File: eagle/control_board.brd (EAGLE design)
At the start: 160 x 100 mm, 24 parts, among them Q1 TIP122V

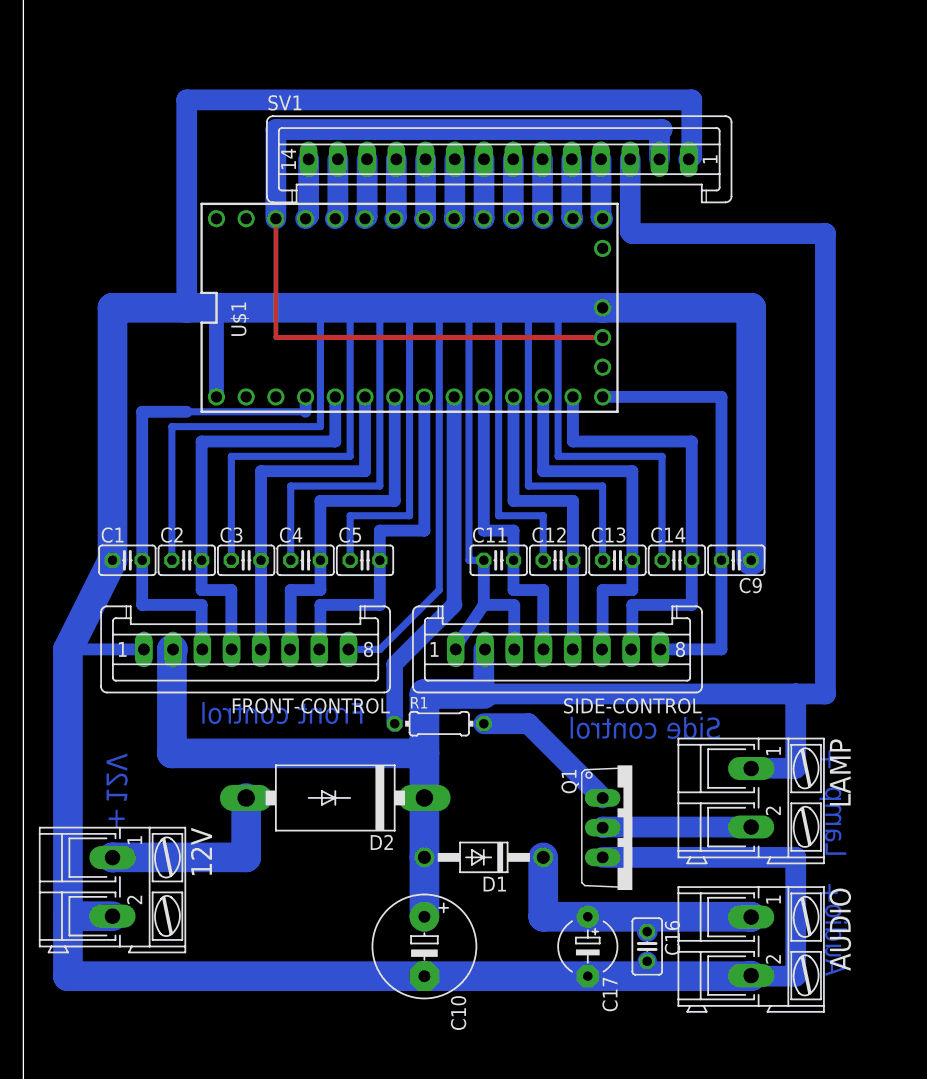
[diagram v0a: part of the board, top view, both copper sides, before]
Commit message: Add USB copy + several bug fix
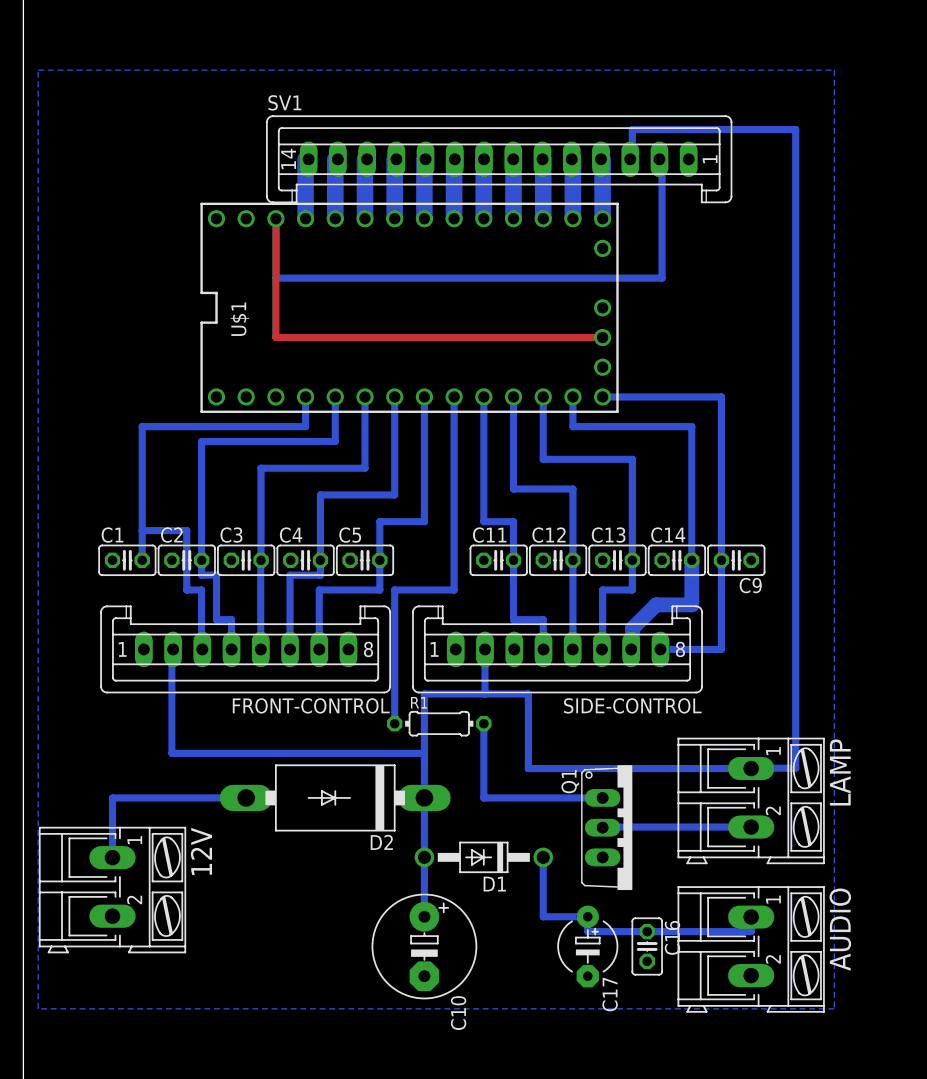
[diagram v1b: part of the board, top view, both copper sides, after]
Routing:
- net GND: track 586.2 -> 0.00 mm
- net +5V: track 81.4 -> 86.6 mm
- net N$1: track 12.8 -> 16.5 mm
- net LAMP: track 30.0 -> 33.0 mm
- net +12V: track 160.2 -> 162.9 mm
- net BTN_PHOTO: track 40.7 -> 43.2 mm
- net N$2: track 24.2 -> 25.4 mm
- net BTN_GAME: track 36.9 -> 35.7 mm
- added copper zone on layer 16, net GND
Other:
- board text removed: "+"
- board text removed: "12V"
- board text removed: "Audio"
- board text removed: "Front control"
- board text removed: "Lamp"
- board text removed: "Side control"

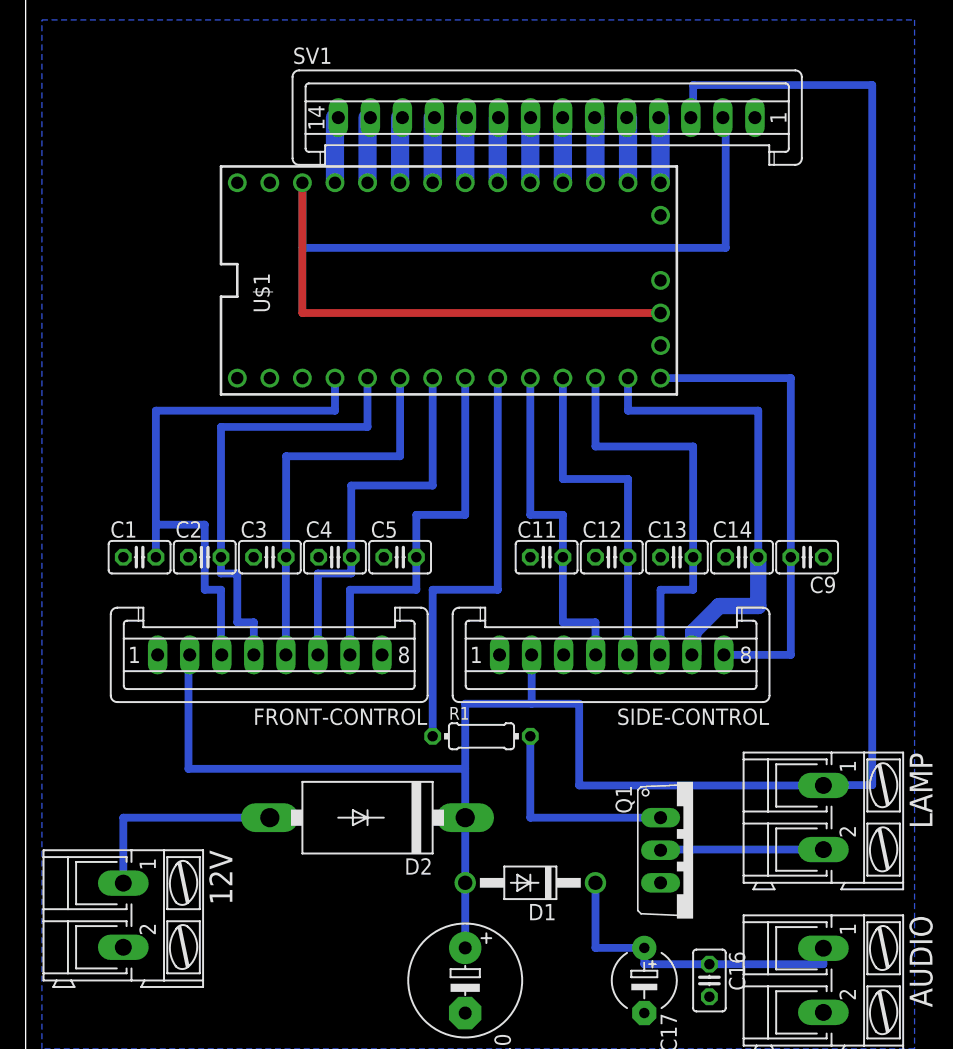
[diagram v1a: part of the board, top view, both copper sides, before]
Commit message: Working form & light control
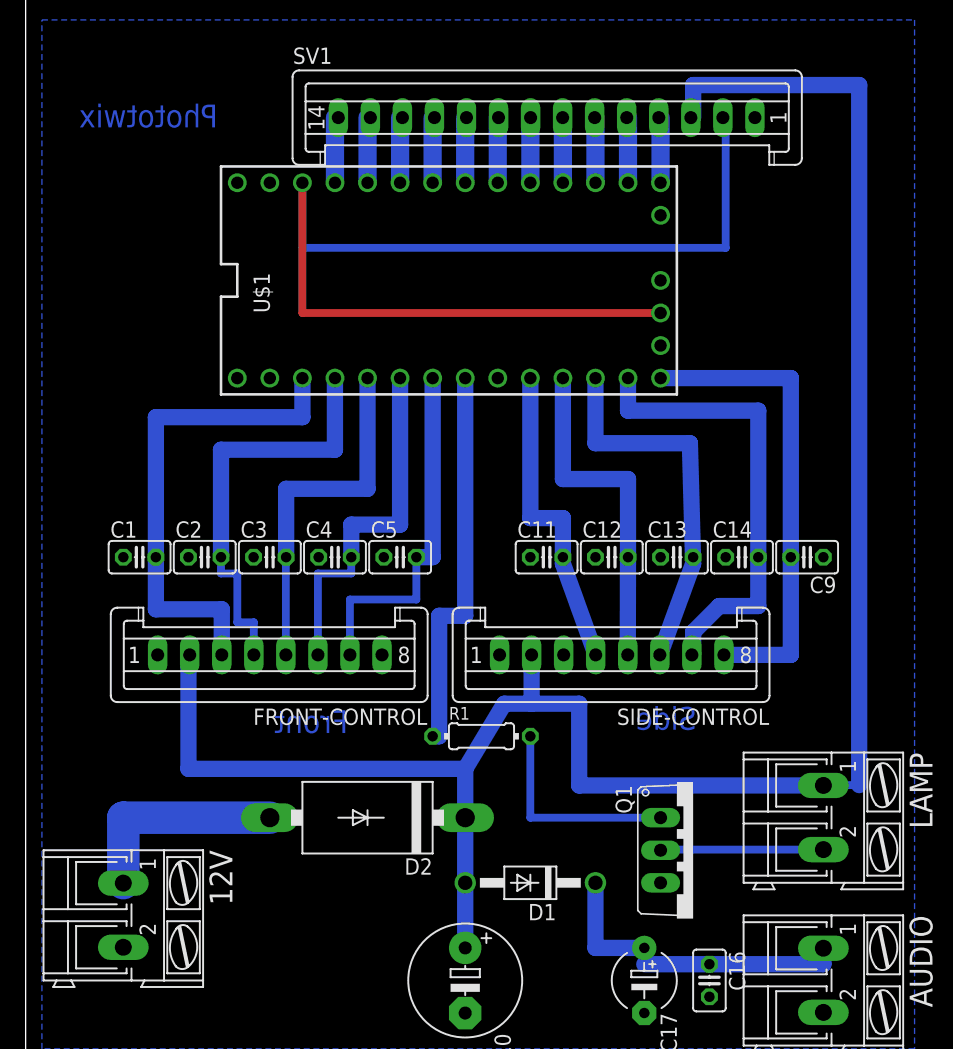
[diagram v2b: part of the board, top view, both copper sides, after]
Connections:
- net BTN_GALLERY: now also U$1.5; no longer U$1.6
- net BTN_NEXT: now also U$1.2; no longer U$1.3
- net BTN_PHOTO: now also U$1.1; no longer U$1.2
- net BTN_PREV: now also U$1.3; no longer U$1.4
- net BTN_TEMPLATE: now also U$1.4; no longer U$1.5
- net LAMP: now also U$1.6; no longer U$1.7
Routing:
- net BTN_PHOTO: track 43.2 -> 38.2 mm
- net +12V: track 162.9 -> 158.7 mm
- net LAMP: track 33.0 -> 30.5 mm
- net BTN_TEMPLATE: track 30.5 -> 28.0 mm
- net BTN_PREV: track 30.5 -> 28.0 mm
- net BTN_NEXT: track 35.6 -> 33.0 mm
- net BTN_GALLERY: track 30.6 -> 28.0 mm
- net BTN_USB: track 31.8 -> 30.0 mm
- net BTN_PRINT: track 26.7 -> 25.1 mm
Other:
- board text added: "Front"
- board text added: "Phototwix"
- board text added: "Side"

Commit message: Autocad plan
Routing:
- net GND: track 0.00 -> 516.1 mm
- net BTN_GALLERY: track 28.0 -> 26.2 mm
- removed copper zone on layer 16, net GND
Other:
- board text added: "12V+"
- board text added: "Audio"
- board text added: "Light+"
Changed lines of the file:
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@@
 <layer number="19" name="Unrouted" color="6" fill="1" visible="yes" active="yes"/>
 <layer number="20" name="Dimension" color="15" fill="1" visible="no" active="yes"/>
-<layer number="21" name="tPlace" color="7" fill="1" visible="yes" active="yes"/>
+<layer number="21" name="tPlace" color="7" fill="1" visible="no" active="yes"/>
 <layer number="22" name="bPlace" color="7" fill="1" visible="no" active="yes"/>
-<layer number="23" name="tOrigins" color="15" fill="1" visible="yes" active="yes"/>
+<layer number="23" name="tOrigins" color="15" fill="1" visible="no" active="yes"/>
 <layer number="24" name="bOrigins" color="15" fill="1" visible="no" active="yes"/>
 <layer number="25" name="tNames" color="7" fill="1" visible="no" active="yes"/>
@@
 <text x="25.146" y="35.814" size="1.778" layer="16" rot="MR0">Front</text>
 <text x="52.324" y="36.068" size="1.778" layer="16" rot="MR0">Side</text>
+<text x="19.304" y="23.368" size="1.778" layer="16" rot="MR0">12V+</text>
+<text x="68.58" y="18.796" size="1.778" layer="16" rot="MR270">Audio</text>
+<text x="68.58" y="29.718" size="1.778" layer="16" rot="MR270">Light+</text>
 </plain>
 <attributes>
@@
 <contactref element="SV1" pad="1"/>
 <contactref element="SIDE-CONTROL" pad="3"/>
-<polygon width="0.6096" layer="16">
-<vertex x="1.27" y="91.44"/>
-<vertex x="69.342" y="91.44"/>
-<vertex x="69.342" y="11.176"/>
-<vertex x="1.27" y="11.176"/>
-</polygon>
+<wire x1="56.89" y1="83.82" x2="57.15" y2="83.82" width="1.27" layer="16"/>
+<wire x1="57.15" y1="83.82" x2="57.15" y2="71.12" width="1.27" layer="16"/>
+<wire x1="57.15" y1="71.12" x2="49.53" y2="71.12" width="1.27" layer="16"/>
+<wire x1="49.53" y1="71.12" x2="45.72" y2="71.12" width="1.27" layer="16"/>
+<wire x1="45.72" y1="71.12" x2="43.18" y2="71.12" width="1.27" layer="16"/>
+<wire x1="43.18" y1="71.12" x2="40.64" y2="71.12" width="1.27" layer="16"/>
+<wire x1="40.64" y1="71.12" x2="35.56" y2="71.12" width="1.27" layer="16"/>
+<wire x1="35.56" y1="71.12" x2="33.02" y2="71.12" width="1.27" layer="16"/>
+<wire x1="33.02" y1="71.12" x2="30.48" y2="71.12" width="1.27" layer="16"/>
+<wire x1="30.48" y1="71.12" x2="27.94" y2="71.12" width="1.27" layer="16"/>
+<wire x1="27.94" y1="71.12" x2="25.4" y2="71.12" width="1.27" layer="16"/>
+<wire x1="25.4" y1="71.12" x2="22.86" y2="71.12" width="1.27" layer="16"/>
+<wire x1="22.86" y1="71.12" x2="16.51" y2="71.12" width="1.27" layer="16"/>
+<wire x1="16.51" y1="71.12" x2="16.51" y2="63.5" width="1.27" layer="16"/>
+<wire x1="7.62" y1="49.53" x2="7.366" y2="49.53" width="1.27" layer="16"/>
+<wire x1="7.366" y1="49.53" x2="7.366" y2="71.12" width="1.27" layer="16"/>
+<wire x1="7.366" y1="71.12" x2="16.51" y2="71.12" width="1.27" layer="16"/>
+<wire x1="62.23" y1="49.53" x2="62.23" y2="71.12" width="1.27" layer="16"/>
+<wire x1="62.23" y1="71.12" x2="57.15" y2="71.12" width="1.27" layer="16"/>
+<wire x1="34.29" y1="13.97" x2="48.26" y2="13.97" width="1.27" layer="16"/>
+<wire x1="48.26" y1="13.97" x2="53.34" y2="13.97" width="1.27" layer="16"/>
+<wire x1="53.34" y1="14.0208" x2="53.34" y2="15.24" width="1.27" layer="16"/>
+<wire x1="62.23" y1="14.0208" x2="53.34" y2="14.0208" width="1.27" layer="16"/>
+<wire x1="53.34" y1="14.0208" x2="53.34" y2="13.97" width="1.27" layer="16"/>
+<wire x1="39.37" y1="49.53" x2="36.97" y2="49.53" width="1.27" layer="16"/>
+<wire x1="36.97" y1="49.53" x2="36.97" y2="45.974" width="1.27" layer="16"/>
+<wire x1="36.97" y1="45.974" x2="36.97" y2="41.91" width="1.27" layer="16"/>
+<wire x1="49.53" y1="24.13" x2="65.278" y2="24.13" width="1.27" layer="16"/>
+<wire x1="65.278" y1="24.13" x2="65.278" y2="14.224" width="1.27" layer="16"/>
+<wire x1="65.278" y1="14.224" x2="62.23" y2="14.224" width="1.27" layer="16"/>
+<wire x1="62.23" y1="14.224" x2="62.23" y2="14.0208" width="1.27" layer="16"/>
+<wire x1="10.3" y1="41.91" x2="7.62" y2="41.91" width="1.27" layer="16"/>
+<wire x1="7.62" y1="41.91" x2="7.62" y2="49.53" width="1.27" layer="16"/>
+<wire x1="12.7" y1="49.53" x2="12.7" y2="59.436" width="0.4064" layer="16"/>
+<wire x1="12.7" y1="59.436" x2="22.86" y2="59.436" width="0.4064" layer="16"/>
+<wire x1="22.86" y1="59.436" x2="22.86" y2="71.12" width="0.4064" layer="16"/>
+<wire x1="17.78" y1="49.53" x2="17.78" y2="56.642" width="0.4064" layer="16"/>
+<wire x1="17.78" y1="56.642" x2="25.4" y2="56.642" width="0.4064" layer="16"/>
+<wire x1="25.4" y1="56.642" x2="25.4" y2="71.12" width="0.4064" layer="16"/>
+<wire x1="22.86" y1="49.53" x2="22.86" y2="53.594" width="0.4064" layer="16"/>
+<wire x1="22.86" y1="53.594" x2="27.94" y2="53.594" width="0.4064" layer="16"/>
+<wire x1="27.94" y1="53.594" x2="27.94" y2="71.12" width="0.4064" layer="16"/>
+<wire x1="27.94" y1="49.53" x2="27.94" y2="50.8" width="0.4064" layer="16"/>
+<wire x1="27.94" y1="50.8" x2="30.48" y2="50.8" width="0.4064" layer="16"/>
+<wire x1="30.48" y1="50.8" x2="30.48" y2="71.12" width="0.4064" layer="16"/>
+<wire x1="27.8" y1="41.91" x2="30.48" y2="41.91" width="0.4064" layer="16"/>
+<wire x1="30.48" y1="41.91" x2="30.48" y2="47.244" width="0.4064" layer="16"/>
+<wire x1="30.48" y1="47.244" x2="33.02" y2="47.244" width="0.4064" layer="16"/>
+<wire x1="33.02" y1="47.244" x2="33.02" y2="71.12" width="0.4064" layer="16"/>
+<wire x1="36.97" y1="49.53" x2="35.56" y2="50.94" width="0.4064" layer="16"/>
+<wire x1="35.56" y1="50.94" x2="35.56" y2="71.12" width="0.4064" layer="16"/>
+<wire x1="41.97" y1="41.91" x2="41.97" y2="43.882" width="0.4064" layer="16"/>
+<wire x1="41.97" y1="43.882" x2="40.132" y2="45.72" width="0.4064" layer="16"/>
+<wire x1="40.132" y1="45.72" x2="37.224" y2="45.72" width="0.4064" layer="16"/>
+<wire x1="37.224" y1="45.72" x2="36.97" y2="45.974" width="0.4064" layer="16"/>
+<wire x1="44.45" y1="49.53" x2="44.45" y2="54.102" width="0.4064" layer="16"/>
+<wire x1="44.45" y1="54.102" x2="40.64" y2="54.102" width="0.4064" layer="16"/>
+<wire x1="40.64" y1="54.102" x2="40.64" y2="71.12" width="0.4064" layer="16"/>
+<wire x1="49.53" y1="49.53" x2="49.53" y2="56.896" width="0.4064" layer="16"/>
+<wire x1="49.53" y1="56.896" x2="43.18" y2="56.896" width="0.4064" layer="16"/>
+<wire x1="43.18" y1="56.896" x2="43.18" y2="71.12" width="0.4064" layer="16"/>
+<wire x1="54.61" y1="49.53" x2="54.61" y2="59.69" width="0.4064" layer="16"/>
+<wire x1="54.61" y1="59.69" x2="45.72" y2="59.69" width="0.4064" layer="16"/>
+<wire x1="45.72" y1="59.69" x2="45.72" y2="71.12" width="0.4064" layer="16"/>
+<wire x1="7.62" y1="19.1008" x2="4.064" y2="19.05" width="1.27" layer="16"/>
+<wire x1="4.064" y1="19.05" x2="4.064" y2="41.91" width="1.27" layer="16"/>
+<wire x1="4.064" y1="41.91" x2="7.62" y2="41.91" width="1.27" layer="16"/>
+<wire x1="34.29" y1="13.97" x2="29.1592" y2="19.1008" width="1.27" layer="16"/>
+<wire x1="29.1592" y1="19.1008" x2="7.62" y2="19.1008" width="1.27" layer="16"/>
 </signal>
 <signal name="BTN_PHOTO">
@@
 <contactref element="C1" pad="2"/>
 <contactref element="U$1" pad="1"/>
-<wire x1="21.59" y1="63.5" x2="21.59" y2="60.452" width="1.27" layer="16"/>
-<wire x1="21.59" y1="60.452" x2="10.16" y2="60.452" width="1.27" layer="16"/>
-<wire x1="10.16" y1="60.452" x2="10.16" y2="49.53" width="1.27" layer="16"/>
+<wire x1="21.59" y1="63.5" x2="21.59" y2="61.214" width="1.27" layer="16"/>
+<wire x1="21.59" y1="61.214" x2="10.16" y2="61.214" width="1.27" layer="16"/>
+<wire x1="10.16" y1="61.214" x2="10.16" y2="49.53" width="1.27" layer="16"/>
 <wire x1="10.16" y1="49.53" x2="10.16" y2="45.466" width="1.27" layer="16"/>
 <wire x1="10.16" y1="45.466" x2="15.3" y2="45.466" width="1.27" layer="16"/>
@@
 <contactref element="FRONT-CONTROL" pad="7"/>
 <contactref element="C5" pad="2"/>
-<wire x1="30.48" y1="49.53" x2="30.48" y2="46.228" width="0.6096" layer="16"/>
-<wire x1="30.48" y1="46.228" x2="25.3" y2="46.228" width="0.6096" layer="16"/>
-<wire x1="25.3" y1="46.228" x2="25.3" y2="41.91" width="0.6096" layer="16"/>
+<wire x1="25.3" y1="46.228" x2="25.3" y2="45.974" width="0.6096" layer="16"/>
 <contactref element="U$1" pad="5"/>
+<wire x1="25.3" y1="45.974" x2="25.3" y2="41.91" width="1.27" layer="16"/>
 <wire x1="31.75" y1="63.5" x2="31.75" y2="49.53" width="1.27" layer="16"/>
 <wire x1="31.75" y1="49.53" x2="30.48" y2="49.53" width="1.27" layer="16"/>
+<wire x1="30.48" y1="49.53" x2="26.924" y2="45.974" width="1.27" layer="16"/>
+<wire x1="26.924" y1="45.974" x2="25.3" y2="45.974" width="1.27" layer="16"/>
 </signal>
 <signal name="BTN_PRINT">
@@
 <wire x1="52.07" y1="86.36" x2="65.024" y2="86.36" width="1.27" layer="16"/>
 <wire x1="65.024" y1="86.36" x2="65.024" y2="31.75" width="1.27" layer="16"/>
-<wire x1="65.024" y1="31.75" x2="62.23" y2="31.75" width="0.6096" layer="16"/>
+<wire x1="65.024" y1="31.75" x2="62.23" y2="31.75" width="1.27" layer="16"/>
 <wire x1="62.23" y1="31.75" x2="62.23" y2="31.7246" width="0.6096" layer="16"/>
 </signal>
